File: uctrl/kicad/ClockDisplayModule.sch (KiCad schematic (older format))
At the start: 9 parts, among them IC1 ATMEGA88PA-A, P101 CONN_02X03, P102 CONN_01X06, SW101 SW_PUSH

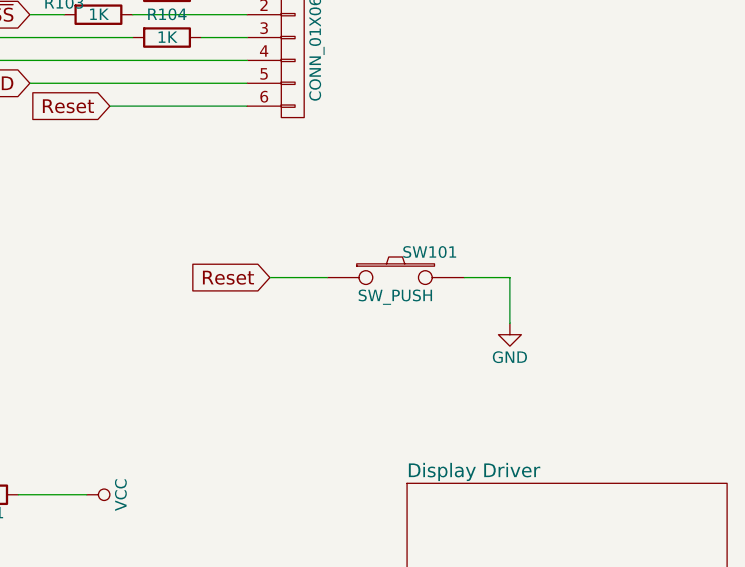
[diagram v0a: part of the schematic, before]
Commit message: Updated the reset switch symbol and footprint
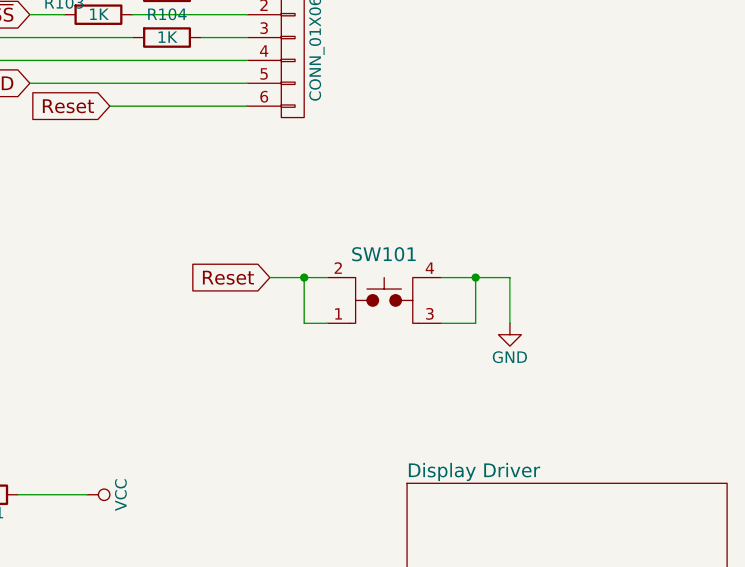
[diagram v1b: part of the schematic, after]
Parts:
- removed SW101: SW_PUSH, ClockFootprints:PTS525SM15SMTR2LFS, symbol SW_PUSH
- added SW101: TL3315NF160Q, ClockFootprints:PTS525SM15SMTR2LFS, symbol TL3315NF160Q
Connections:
- net GND: now also SW101.3, SW101.4
- net Reset: now also SW101.1, SW101.2
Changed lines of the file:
@@
 Wire Wire Line
 	2250 1750 2250 2200
-$Comp
-L SW_PUSH SW101
-U 1 1 5660EB7E
-P 7800 2700
-F 0 "SW101" H 7950 2810 50  0000 C CNN
-F 1 "SW_PUSH" H 7800 2620 50  0000 C CNN
-F 2 "ClockFootprints:PTS525SM15SMTR2LFS" H 7800 2700 60  0001 C CNN
-F 3 "" H 7800 2700 60  0000 C CNN
-	1    7800 2700
-	1    0    0    -1
-$EndComp
 Text GLabel 7250 2700 0    60   Input ~ 0
 Reset
@@
 	7250 2700 7500 2700
 Wire Wire Line
-	8100 2700 8300 2700
+	8000 2700 8300 2700
 Wire Wire Line
 	8300 2700 8300 2900
+$Comp
+L TL3315NF160Q SW101
+U 1 1 566C8241
+P 7500 2900
+F 0 "SW101" V 7800 2650 60  0000 C CNN
+F 1 "TL3315NF160Q" H 8125 2650 60  0001 C CNN
+F 2 "ClockFootprints:PTS525SM15SMTR2LFS" H 7600 2600 60  0001 C CNN
+F 3 "" H 7600 2600 60  0000 C CNN
+	1    7500 2900
+	0    -1   -1   0
+$EndComp
+Wire Wire Line
+	8000 2900 8150 2900
+Wire Wire Line
+	8150 2900 8150 2700
+Connection ~ 8150 2700
+Wire Wire Line
+	7500 2900 7400 2900
+Wire Wire Line
+	7400 2900 7400 2700
+Connection ~ 7400 2700
 $EndSCHEMATC

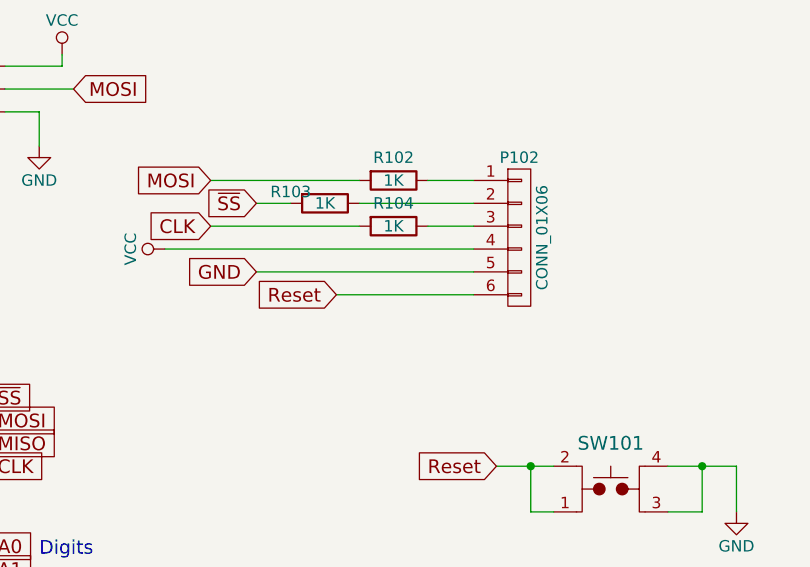
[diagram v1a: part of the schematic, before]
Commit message: Finished routing of revision 4
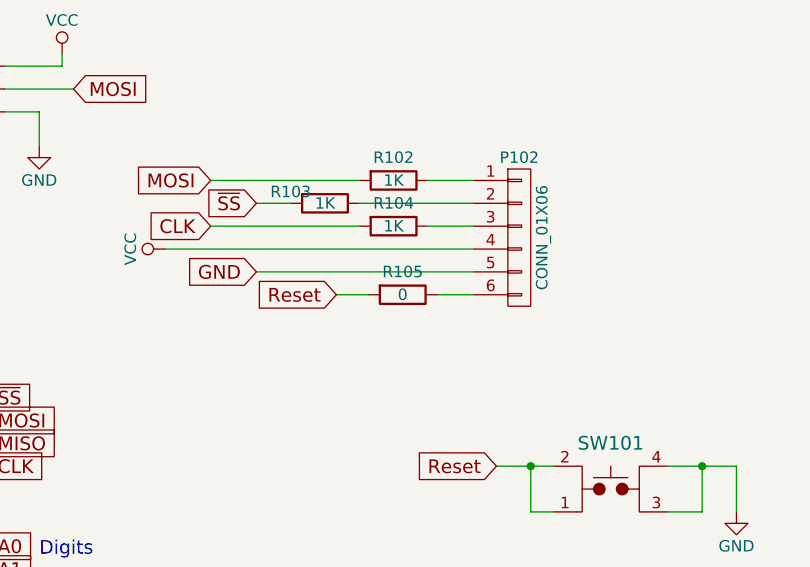
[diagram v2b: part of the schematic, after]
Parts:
- added R105: 0, Resistors_SMD:R_0805, symbol R
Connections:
- net Reset: now also R105.2; no longer P102.6 (P6)
- new net: P102.6 (P6), R105.1
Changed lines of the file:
@@
 $EndComp
 NoConn ~ 4750 4500
-Wire Wire Line
-	4750 3800 5100 3800
-Wire Wire Line
-	4750 3900 5100 3900
-Wire Wire Line
-	4750 4000 5100 4000
-Wire Wire Line
-	4750 4100 5100 4100
-Wire Wire Line
-	5800 1750 7150 1750
-Wire Wire Line
-	6200 1850 7150 1850
-Wire Wire Line
-	5000 3050 4750 3050
-Wire Wire Line
-	5000 3150 4750 3150
-Wire Wire Line
-	4750 3250 5000 3250
-Wire Wire Line
-	4750 2700 5000 2700
-Wire Wire Line
-	4750 2500 5000 2500
-Wire Wire Line
-	4750 2400 5000 2400
-Wire Wire Line
-	2850 4300 2400 4300
-Wire Wire Line
-	2400 4300 2400 4550
-Wire Wire Line
-	5350 900  5350 950
-Wire Wire Line
-	5350 950  5100 950
-Wire Wire Line
-	5100 1150 5250 1150
-Wire Wire Line
-	5250 1150 5250 1300
-Wire Wire Line
-	5100 1050 5400 1050
-Wire Wire Line
-	4600 950  4400 950
-Wire Wire Line
-	4600 1050 4400 1050
-Wire Wire Line
-	4400 1150 4600 1150
-Wire Wire Line
-	4750 2600 5000 2600
-Wire Wire Line
-	2850 4400 2400 4400
-Connection ~ 2400 4400
-Wire Wire Line
-	2850 4500 2400 4500
-Connection ~ 2400 4500
 $Comp
 L GND #PWR06
@@
 	1    0    0    -1
 $EndComp
-Wire Wire Line
-	2600 2900 2600 3000
-Wire Wire Line
-	2750 2200 2750 2500
-Wire Wire Line
-	2750 2300 2850 2300
-Connection ~ 2750 2200
-Wire Wire Line
-	2250 2200 2850 2200
-Wire Wire Line
-	2750 2500 2850 2500
-Connection ~ 2750 2300
-Wire Wire Line
-	2600 2600 2600 2200
-Connection ~ 2600 2200
 NoConn ~ 2850 2800
 NoConn ~ 4750 2200
@@
 Text GLabel 5600 3400 2    60   Input ~ 0
 Reset
-Wire Wire Line
-	4750 3650 5850 3650
-Wire Wire Line
-	5300 3650 5300 3400
-Wire Wire Line
-	5300 3400 5600 3400
 $Comp
 L R R101
@@
 	0    1    1    0
 $EndComp
-Connection ~ 5300 3650
 $Comp
 L VCC #PWR07
@@
 	0    1    1    0
 $EndComp
-Wire Wire Line
-	6450 3650 6150 3650
 $Comp
 L R R102
@@
 	0    1    1    0
 $EndComp
-Wire Wire Line
-	6000 1450 6650 1450
-Wire Wire Line
-	6950 1450 7150 1450
-Wire Wire Line
-	7150 1550 6650 1550
-Wire Wire Line
-	6350 1550 6200 1550
-Wire Wire Line
-	6000 1650 6650 1650
-Wire Wire Line
-	6950 1650 7150 1650
 $Comp
 L CONN_01X06 P102
@@
 Text GLabel 6550 1950 0    60   Input ~ 0
 Reset
-Wire Wire Line
-	6550 1950 7150 1950
-Wire Wire Line
-	2250 1750 2250 2200
 Text GLabel 7250 2700 0    60   Input ~ 0
 Reset
@@
 	1    0    0    -1
 $EndComp
-Wire Wire Line
-	7250 2700 7500 2700
-Wire Wire Line
-	8000 2700 8300 2700
-Wire Wire Line
-	8300 2700 8300 2900
 $Comp
 L TL3315NF160Q SW101
@@
 	0    -1   -1   0
 $EndComp
+$Comp
+L R R105
+U 1 1 56DAA348
+P 6840 1950
+F 0 "R105" V 6740 1950 50  0000 C CNN
+F 1 "0" V 6840 1950 50  0000 C CNN
+F 2 "Resistors_SMD:R_0805" V 6770 1950 30  0001 C CNN
+F 3 "" H 6840 1950 30  0000 C CNN
+	1    6840 1950
+	0    1    1    0
+$EndComp
+Wire Wire Line
+	4750 3800 5100 3800
+Wire Wire Line
+	4750 3900 5100 3900
+Wire Wire Line
+	4750 4000 5100 4000
+Wire Wire Line
+	4750 4100 5100 4100
+Wire Wire Line
+	5800 1750 7150 1750
+Wire Wire Line
+	6200 1850 7150 1850
+Wire Wire Line
+	5000 3050 4750 3050
+Wire Wire Line
+	5000 3150 4750 3150
+Wire Wire Line
+	4750 3250 5000 3250
+Wire Wire Line
+	4750 2700 5000 2700
+Wire Wire Line
+	4750 2500 5000 2500
+Wire Wire Line
+	4750 2400 5000 2400
+Wire Wire Line
+	2850 4300 2400 4300
+Wire Wire Line
+	2400 4300 2400 4550
+Wire Wire Line
+	5350 900  5350 950
+Wire Wire Line
+	5350 950  5100 950
+Wire Wire Line
+	5100 1150 5250 1150
+Wire Wire Line
+	5250 1150 5250 1300
+Wire Wire Line
+	5100 1050 5400 1050
+Wire Wire Line
+	4600 950  4400 950
+Wire Wire Line
+	4600 1050 4400 1050
+Wire Wire Line
+	4400 1150 4600 1150
+Wire Wire Line
+	4750 2600 5000 2600
+Wire Wire Line
+	2850 4400 2400 4400
+Connection ~ 2400 4400
+Wire Wire Line
+	2850 4500 2400 4500
+Connection ~ 2400 4500
+Wire Wire Line
+	2600 2900 2600 3000
+Wire Wire Line
+	2750 2200 2750 2500
+Wire Wire Line
+	2750 2300 2850 2300
+Connection ~ 2750 2200
+Wire Wire Line
+	2250 2200 2850 2200
+Wire Wire Line
+	2750 2500 2850 2500
+Connection ~ 2750 2300
+Wire Wire Line
+	2600 2600 2600 2200
+Connection ~ 2600 2200
+Wire Wire Line
+	4750 3650 5850 3650
+Wire Wire Line
+	5300 3650 5300 3400
+Wire Wire Line
+	5300 3400 5600 3400
+Connection ~ 5300 3650
+Wire Wire Line
+	6450 3650 6150 3650
+Wire Wire Line
+	6000 1450 6650 1450
+Wire Wire Line
+	6950 1450 7150 1450
+Wire Wire Line
+	7150 1550 6650 1550
+Wire Wire Line
+	6350 1550 6200 1550
+Wire Wire Line
+	6000 1650 6650 1650
+Wire Wire Line
+	6950 1650 7150 1650
+Wire Wire Line
+	2250 1750 2250 2200
+Wire Wire Line
+	7250 2700 7500 2700
+Wire Wire Line
+	8000 2700 8300 2700
+Wire Wire Line
+	8300 2700 8300 2900
 Wire Wire Line
 	8000 2900 8150 2900
@@
 	7400 2900 7400 2700
 Connection ~ 7400 2700
+Wire Wire Line
+	6550 1950 6690 1950
+Wire Wire Line
+	6990 1950 7150 1950
 $EndSCHEMATC
